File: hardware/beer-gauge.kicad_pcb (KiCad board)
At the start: 4 copper layers, 69.8 x 95.2 mm, 58 parts, among them J1 OLED_MODULE, P1 CONN_01X04, P2 CONN_01X04, P3 CONN_01X04, P4 CONN_01X04, P5 USB_OTG, SW1 SW_PUSH, U1 ADS1234IPW, U2 LP38691, U3 MKL02Z32, U4 MK20DX256VLH7, Y1 16 MHz, Y2 32.768 kHz

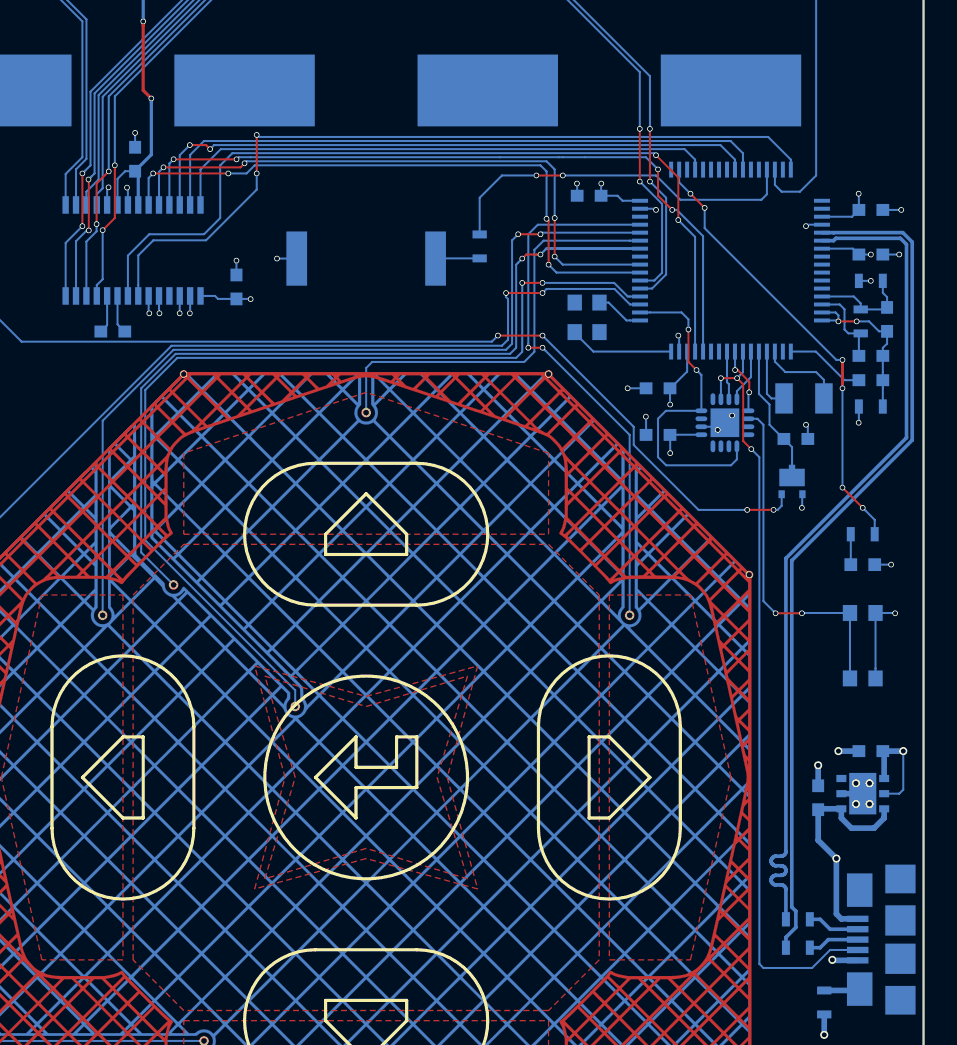
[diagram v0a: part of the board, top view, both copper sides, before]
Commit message: Added some silkscreen text.  Adjusted soldermask clearance as it was too large.
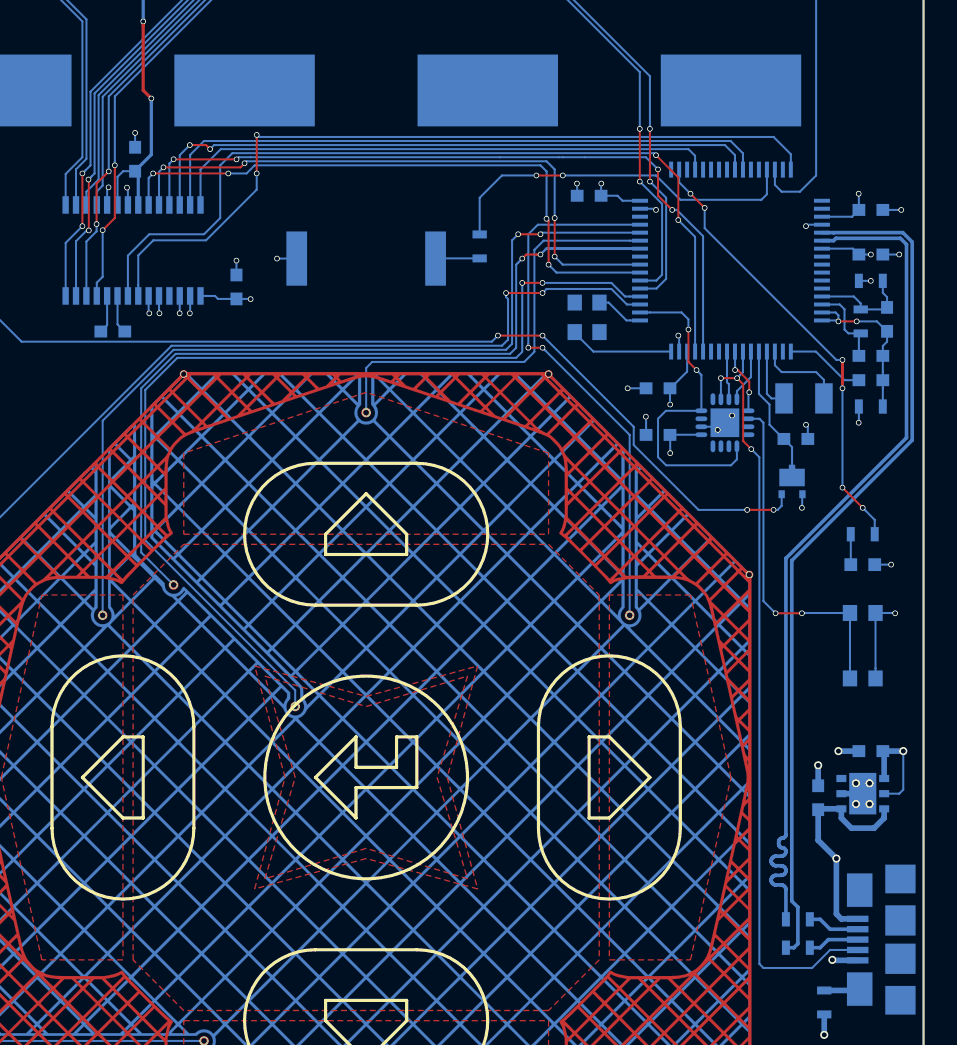
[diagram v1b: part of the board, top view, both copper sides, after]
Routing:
- net /Teensy/USB_D-: track 53.6 -> 54.1 mm
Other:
- rule pad_to_mask_clearance: 0.2 -> 0.0635
- board text added: "AIN1"
- board text added: "AIN2"
- board text added: "AIN3"
- board text added: "AIN4"
- board text added: "Kegerator Beer Gauge"
- board text added: "https://github.com/jeffkub/beer-gauge"

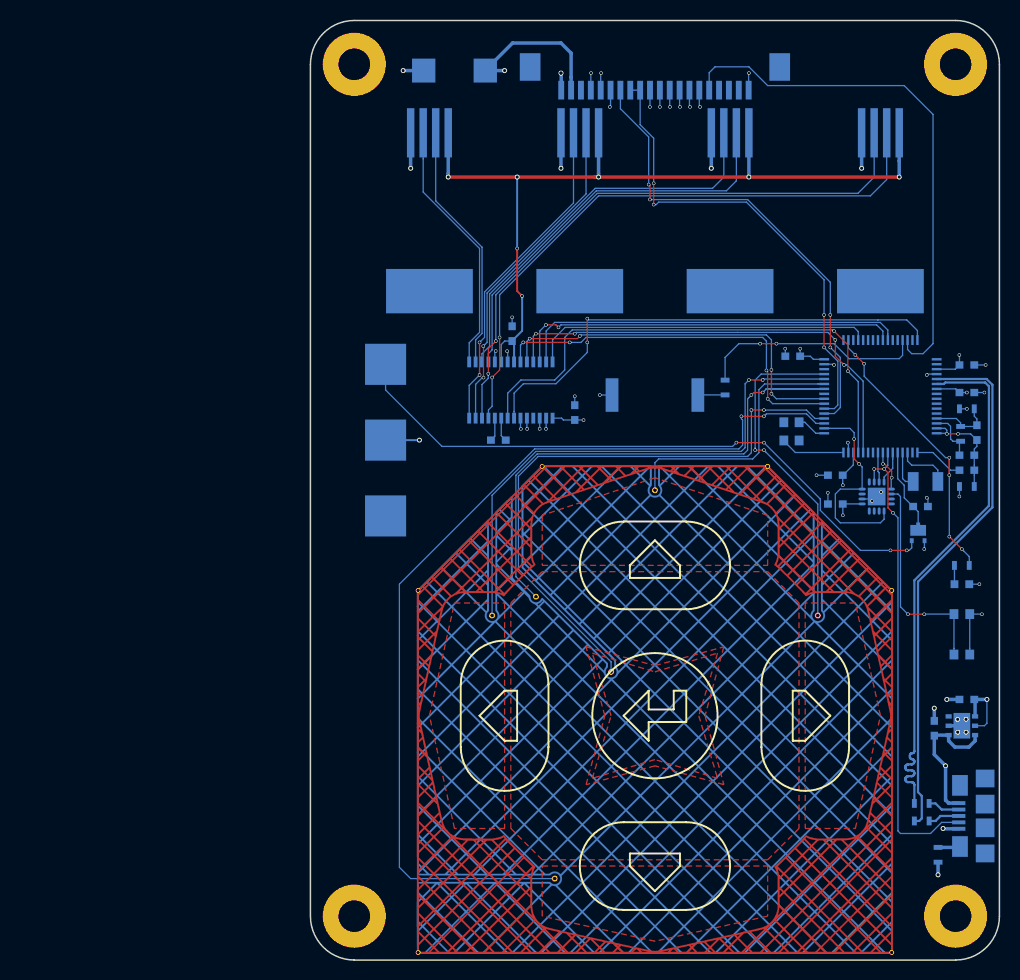
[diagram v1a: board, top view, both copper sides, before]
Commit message: Updating schematic/BOM to use 2 channel ADC, added I2C switch
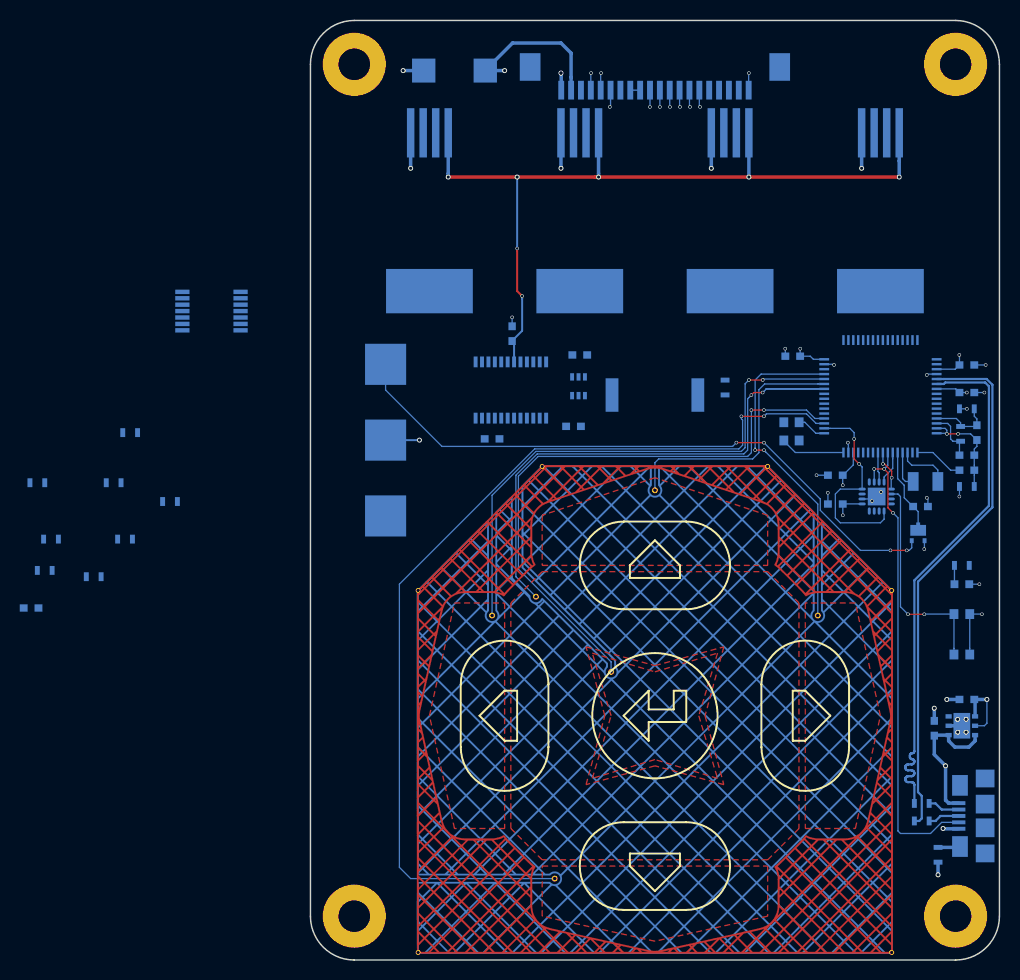
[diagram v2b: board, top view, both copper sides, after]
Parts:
- added C16: 0.1u, Capacitors_SMD:C_0603, B.Cu at (108.8, 105.3)
- added C17: 0.1u, Capacitors_SMD:C_0603, B.Cu at (164.5, 79.6)
- added R10: 4.7k, Resistors_SMD:R_0603, B.Cu at (109.5, 92.6)
- added R11: 4.7k, Resistors_SMD:R_0603, B.Cu at (117.2, 92.6)
- added R12: 4.7k, Resistors_SMD:R_0603, B.Cu at (122.9, 94.5)
- added R13: 4.7k, Resistors_SMD:R_0603, B.Cu at (118.9, 87.5)
- added R6: 4.7k, Resistors_SMD:R_0603, B.Cu at (110.2, 101.5)
- added R7: 4.7k, Resistors_SMD:R_0603, B.Cu at (115.2, 102.1)
- added R8: 4.7k, Resistors_SMD:R_0603, B.Cu at (110.9, 98.3)
- added R9: 4.7k, Resistors_SMD:R_0603, B.Cu at (118.4, 98.3)
- added U5: TCA9543A, Housings_SSOP:TSSOP-14_4.4x5mm_Pitch0.65mm, B.Cu at (127.1, 75.2)
- added U6: SN74LVC1G58, TO_SOT_Packages_SMD:SC-70-6, B.Cu at (164.3, 82.8)
- U1: value ADS1234IPW -> ADS1232IPW; footprint Housings_SSOP:TSSOP-28_4.4x9.7mm_Pitch0.65mm -> Housings_SSOP:TSSOP-24_4.4x7.8mm_Pitch0.65mm
- moved C2 1.40 mm to (163.8, 86.9), turned to 0 degrees
- moved C3 0.65 mm to (155.6, 88.1)
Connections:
- J1 pad 15: GND -> /Teensy/10
- J1 pad 16: /Teensy/20/A6 -> /Teensy/8
- J1 pad 4: GND -> /Teensy/9
- J1 pad 7: /Teensy/19/A5 -> /Teensy/13
- J1 pad 8: /Teensy/18/A4 -> /Teensy/11
- J1 pad 9: /Teensy/18/A4 -> (no net)
- R1 pad 1: /Teensy/13 -> /Teensy/20/A6
- U1 pad 13: Net-(P3-Pad2) -> Net-(P2-Pad3)
- U1 pad 14: Net-(P3-Pad3) -> Net-(P2-Pad2)
- U1 pad 15: Net-(P4-Pad3) -> GND
- U1 pad 16: Net-(P4-Pad2) -> +5V
- U1 pad 17: Net-(P2-Pad3) -> GND
- U1 pad 18: Net-(P2-Pad2) -> +5V
- U1 pad 19: GND -> /Teensy/0
- U1 pad 20: +5V -> /Teensy/1
- U1 pad 21: GND -> /Teensy/3
- U1 pad 22: +5V -> /Teensy/2
- U1 pad 23: /Teensy/0 -> Net-(U1-Pad23)
- U1 pad 24: /Teensy/1 -> /Teensy/12
- U4 pad 46: (no net) -> /Teensy/9
- U4 pad 49: (no net) -> /Teensy/10
- U4 pad 51: (no net) -> /Teensy/11
- U4 pad 58: /Teensy/14/A0 -> (no net)
- U4 pad 59: (no net) -> /Teensy/7
- U4 pad 60: (no net) -> /Teensy/8
- U4 pad 63: (no net) -> /Teensy/21/A7
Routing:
- net Net-(P1-Pad2): track 61.8 -> 0.00 mm, vias 2 -> 0
- net Net-(P1-Pad3): track 60.9 -> 0.00 mm, vias 2 -> 0
- net /Teensy/20/A6: track 54.1 -> 0.00 mm
- net /Teensy/4: track 53.6 -> 0.00 mm, vias 2 -> 0
- net /Teensy/5: track 50.0 -> 0.00 mm, vias 2 -> 0
- net /Teensy/19/A5: track 49.1 -> 0.00 mm, vias 4 -> 0
- net /Teensy/18/A4: track 48.6 -> 0.00 mm, vias 4 -> 0
- net /Teensy/3: track 46.5 -> 0.00 mm, vias 4 -> 0
- net Net-(P2-Pad2): track 41.4 -> 0.00 mm
- net Net-(P2-Pad3): track 42.5 -> 2.12 mm
- net /Teensy/2: track 39.6 -> 0.00 mm, vias 2 -> 0
- net /Teensy/14/A0: track 39.5 -> 0.00 mm
- net /Teensy/0: track 38.9 -> 0.00 mm, vias 4 -> 0
- net /Teensy/1: track 38.4 -> 0.00 mm, vias 4 -> 0
- net /Teensy/12: track 34.8 -> 0.00 mm
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
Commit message: Updating layout with schematic changes
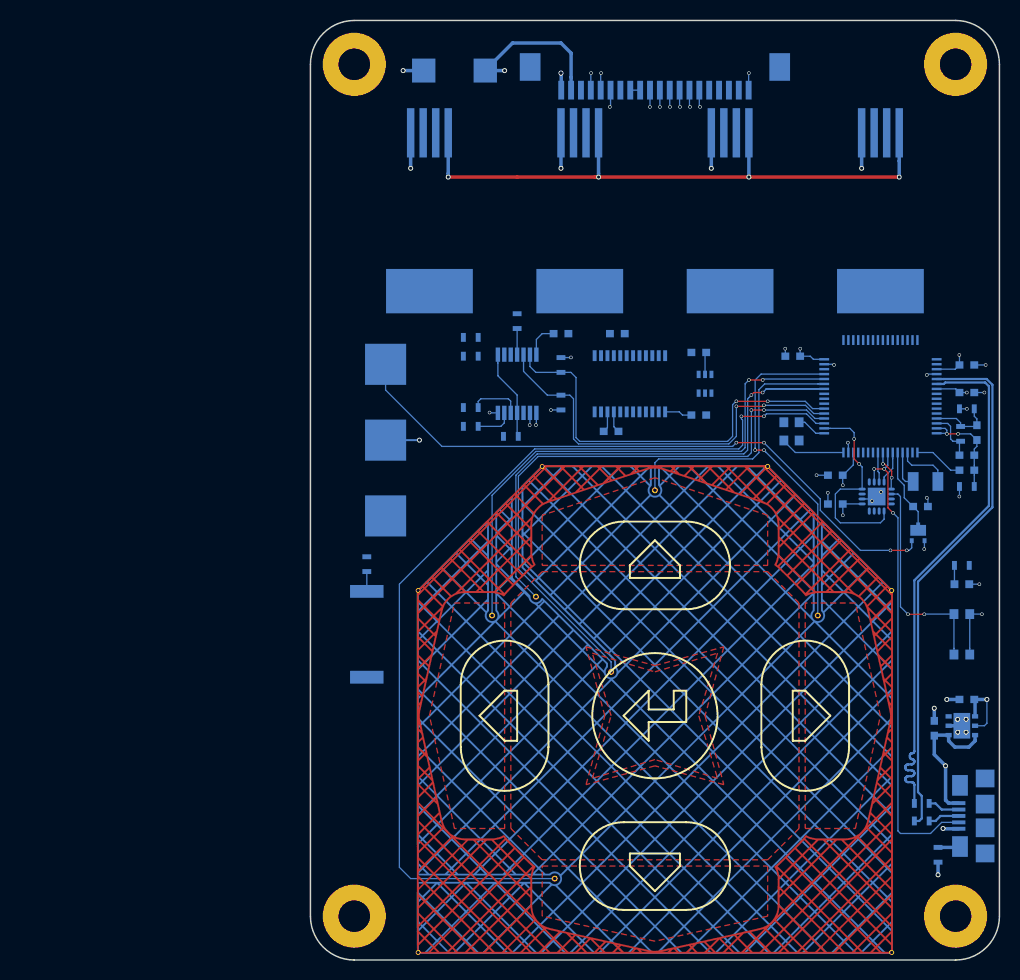
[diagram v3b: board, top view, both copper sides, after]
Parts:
- U1: value ADS1232IPW -> ADS1232
- moved C16 60.5 mm to (162.6, 77.5)
- moved R6 56.3 mm to (162.6, 80.6), turned to 270 degrees
- moved R8 52.2 mm to (158.1, 76.2), turned to 270 degrees
- moved R7 50.6 mm to (162.6, 84.5), turned to 90 degrees
- moved R10 44.6 mm to (153.4, 85.0)
- moved R5 40.5 mm to (142.9, 100.8)
- moved R9 40.5 mm to (157.5, 87.9)
- moved R11 38.4 mm to (153.4, 79.8)
- moved SP1 38.0 mm to (142.9, 108.0), turned to 270 degrees
- moved R13 35.9 mm to (153.4, 77.9)
- moved U5 31.9 mm to (158.1, 82.5), turned to 90 degrees
- moved R12 31.4 mm to (153.4, 86.9)
- moved U6 12.8 mm to (177.2, 82.5)
- moved C2 12.8 mm to (176.5, 85.7)
- moved C3 12.1 mm to (167.6, 87.4)
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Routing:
- net /Teensy/18/A4: track 0.00 -> 41.6 mm, vias 0 -> 2
- net /Teensy/19/A5: track 0.00 -> 41.4 mm, vias 0 -> 2
- net +5V: track 164.8 -> 145.4 mm, vias 8 -> 5
- net +3V3: track 41.4 -> 52.0 mm, vias 9 -> 11
- net Net-(R9-Pad2): track 0.00 -> 9.14 mm
- net Net-(P3-Pad3): track 0.00 -> 5.32 mm
- net Net-(P3-Pad2): track 0.00 -> 3.81 mm
- net Net-(R8-Pad2): track 0.00 -> 2.65 mm
- net GND: track 62.8 -> 65.2 mm, vias 38 -> 40
- net Net-(C3-Pad1): track 0.00 -> 2.17 mm
- net Net-(C3-Pad2): track 0.00 -> 2.13 mm
- net Net-(R5-Pad1): track 0.02 -> 2.01 mm

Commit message: Finished layout of traces
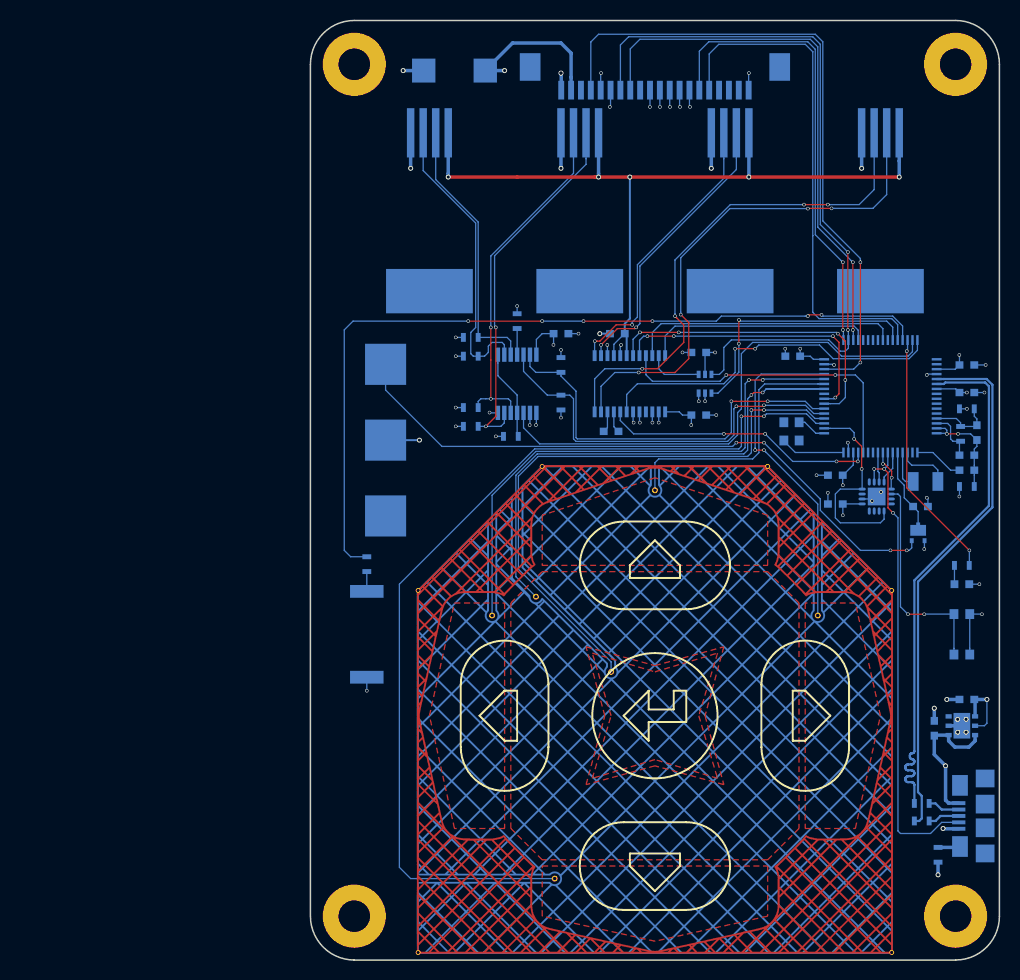
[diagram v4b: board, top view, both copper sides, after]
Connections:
- R10 pad 1: +5V -> +3V3
- R11 pad 1: +5V -> +3V3
- R12 pad 1: +5V -> +3V3
- R13 pad 1: +5V -> +3V3
- R9 pad 1: +5V -> +3V3
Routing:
- net /Teensy/6: track 0.00 -> 84.0 mm, vias 0 -> 6
- net /Teensy/13: track 0.00 -> 74.8 mm, vias 0 -> 2
- net /Teensy/9: track 1.74 -> 67.1 mm, vias 1 -> 2
- net /Teensy/11: track 1.00 -> 55.1 mm, vias 0 -> 2
- net Net-(P1-Pad2): track 0.00 -> 53.0 mm, vias 0 -> 4
- net /Teensy/21/A7: track 0.00 -> 52.4 mm
- net /Teensy/8: track 0.00 -> 52.0 mm
- net Net-(P1-Pad3): track 0.00 -> 51.6 mm, vias 0 -> 4
- net /Teensy/10: track 1.73 -> 47.1 mm, vias 1 -> 2
- net /Teensy/5: track 0.00 -> 36.7 mm, vias 0 -> 2
- net Net-(P3-Pad2): track 3.81 -> 37.9 mm, vias 0 -> 2
- net /Teensy/0: track 0.00 -> 32.0 mm, vias 0 -> 4
- net /Teensy/3: track 0.00 -> 31.9 mm, vias 0 -> 2
- net Net-(P3-Pad3): track 5.32 -> 35.8 mm, vias 0 -> 2
- net Net-(P4-Pad3): track 0.00 -> 30.4 mm
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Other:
- board text added: "I2C1"
- board text added: "I2C2"
- board text removed: "AIN3"
- board text removed: "AIN4"

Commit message: Minor fixes to layout
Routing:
- net +3V3: track 59.2 -> 61.3 mm
- net GND: track 78.9 -> 78.8 mm, vias 53 -> 54
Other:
- board text added: "SCALE 1"
- board text added: "SCALE 2"
- board text added: "SENSOR 1"
- board text added: "SENSOR 2"
- board text removed: "AIN1"
- board text removed: "AIN2"
- board text removed: "I2C1"
- board text removed: "I2C2"
